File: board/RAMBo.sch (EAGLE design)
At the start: 287 parts, among them Q1 PSMN7R0-60YS, Q2 PSMN7R0-60YS, Q3 PSMN7R0-60YS, Q4 IRLML6346TRPBF, Q5 PSMN7R0-60YS, Q8 IRLML6346TRPBF, U1 ATMEGA32U2-MUR, U10 ADUM7441, U2 ATMEGA2560-16AU, U3 LM22675, U4 AD5206, U5 A4982, U6 A4982, U7 A4982, U8 A4982, U9 A4982, X1 C-GRID-02-70543, X10 C-GRID-04-70543, X11 MSTBV10, X12 SPI, X13 EXT-2, X14 C-GRID-04-70543, X15 C-GRID-04-70543, X16 32u2 EXT, X17 3x2M, X18 3x2M, X2 USB B-TH, X20 MX1, X21 C-GRID-03-70543, X22 C-GRID-03-70543, X23 C-GRID-03-70543, X24 C-GRID-03-70543, X25 C-GRID-03-70543, X26 C-GRID-03-70543, X27 C-GRID-02-70543, X28 C-GRID-02-70543, X29 C-GRID-02-70543, X3 C-GRID-02-70543, X30 C-GRID-02-70543, X31 MX2, X32 MX3, X33 MSTBA6, X34 PWM_EXT, X39 M05X2PTH, X4 C-GRID-04-70543, X40 Analog, X5 C-GRID-02-70543, X6 C-GRID-04-70543, X7 C-GRID-04-70543, X8 C-GRID-04-70543, X9 C-GRID-02-70543, Y1 16MHz KX-7, Y2 16MHz KX-7

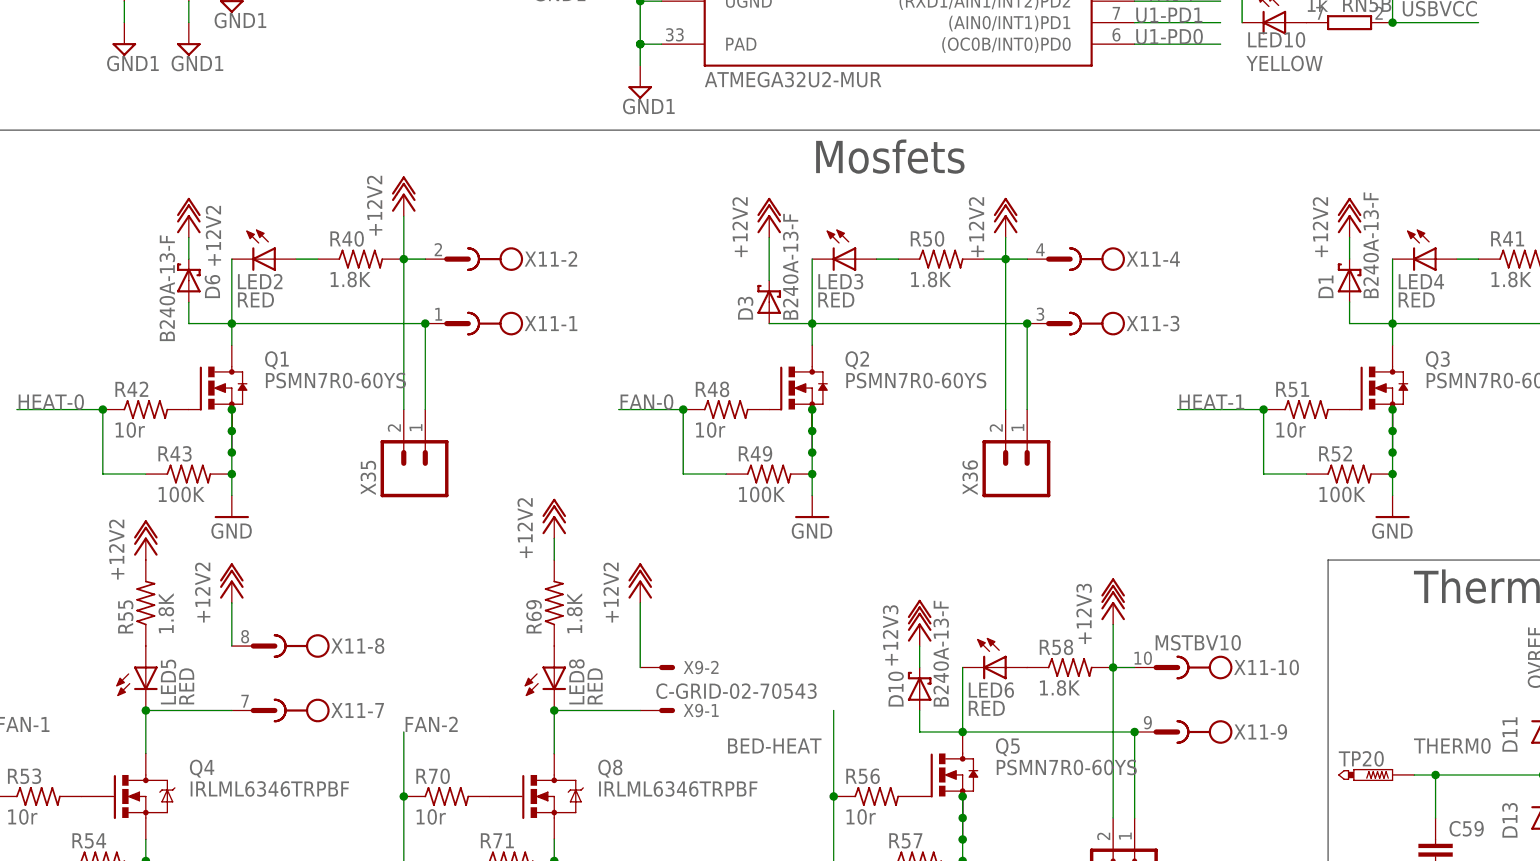
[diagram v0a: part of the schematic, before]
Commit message: Change flyback diodes to SK310A
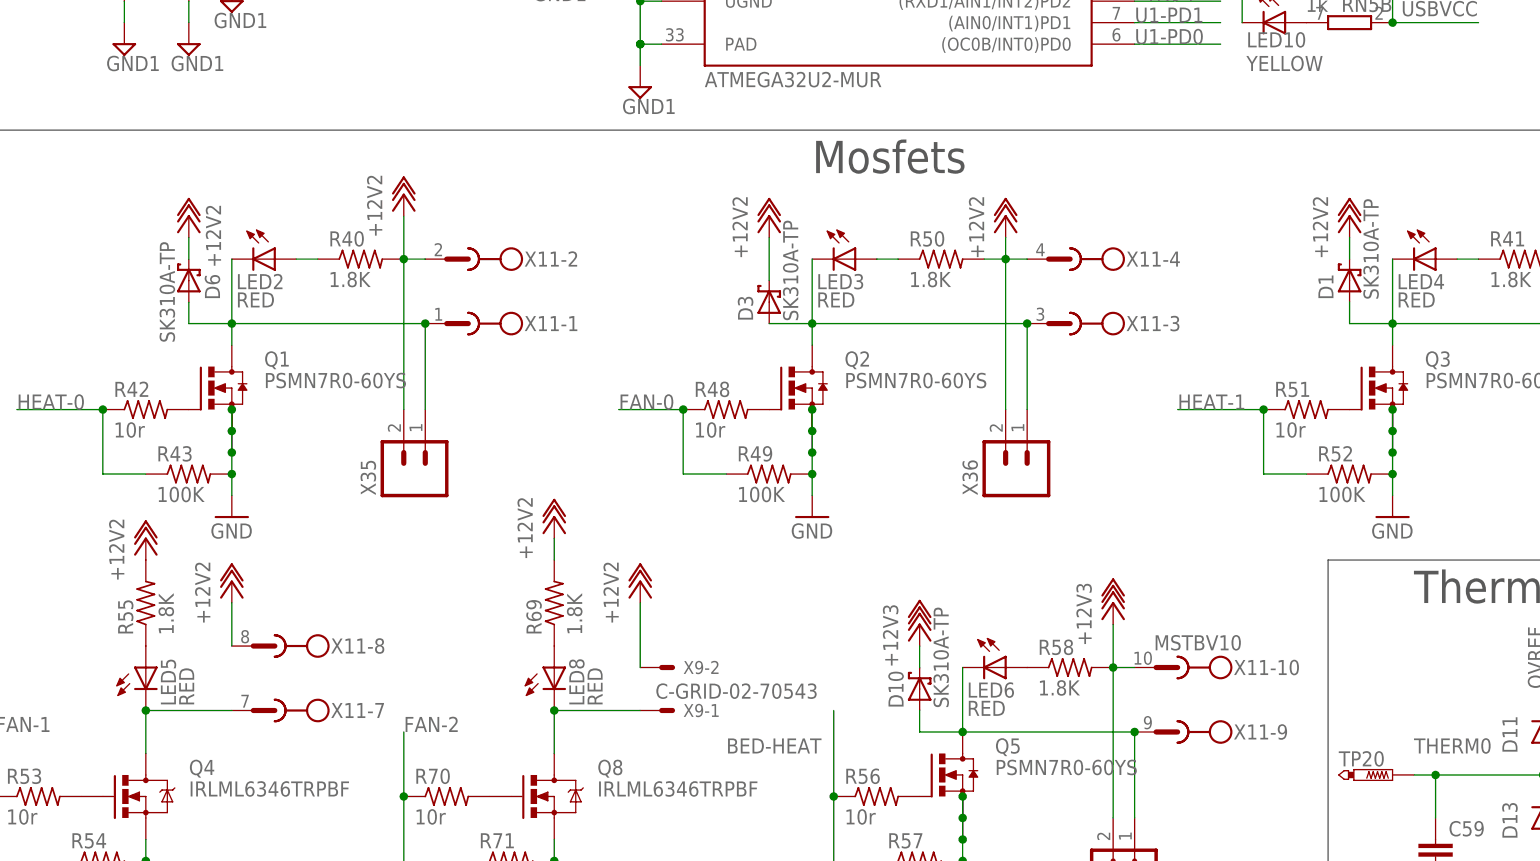
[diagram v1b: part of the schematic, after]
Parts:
- D1, D10, D3, D6: value B240A-13-F -> SK310A-TP
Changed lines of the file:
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@@
 <grid distance="0.1" unitdist="inch" unit="inch" style="lines" multiple="1" display="no" altdistance="0.01" altunitdist="inch" altunit="inch"/>
 <layers>
-<layer number="1" name="Top" color="4" fill="1" visible="yes" active="no"/>
-<layer number="2" name="Route2" color="13" fill="3" visible="yes" active="no"/>
-<layer number="3" name="Route3" color="4" fill="3" visible="yes" active="no"/>
-<layer number="14" name="Route14" color="1" fill="6" visible="yes" active="no"/>
-<layer number="15" name="Route15" color="11" fill="6" visible="yes" active="no"/>
-<layer number="16" name="Bottom" color="1" fill="1" visible="yes" active="no"/>
-<layer number="17" name="Pads" color="2" fill="1" visible="yes" active="no"/>
-<layer number="18" name="Vias" color="2" fill="1" visible="yes" active="no"/>
-<layer number="19" name="Unrouted" color="6" fill="1" visible="yes" active="no"/>
-<layer number="20" name="Dimension" color="15" fill="1" visible="yes" active="no"/>
-<layer number="21" name="tPlace" color="7" fill="1" visible="yes" active="no"/>
-<layer number="22" name="bPlace" color="7" fill="1" visible="yes" active="no"/>
-<layer number="23" name="tOrigins" color="15" fill="1" visible="yes" active="no"/>
-<layer number="24" name="bOrigins" color="15" fill="1" visible="yes" active="no"/>
-<layer number="25" name="tNames" color="7" fill="1" visible="yes" active="no"/>
-<layer number="26" name="bNames" color="7" fill="1" visible="yes" active="no"/>
-<layer number="27" name="tValues" color="7" fill="1" visible="yes" active="no"/>
-<layer number="28" name="bValues" color="7" fill="1" visible="yes" active="no"/>
+<layer number="1" name="Top" color="4" fill="1" visible="no" active="no"/>
+<layer number="2" name="Route2" color="13" fill="3" visible="no" active="no"/>
+<layer number="3" name="Route3" color="4" fill="3" visible="no" active="no"/>
+<layer number="14" name="Route14" color="1" fill="6" visible="no" active="no"/>
+<layer number="15" name="Route15" color="11" fill="6" visible="no" active="no"/>
+<layer number="16" name="Bottom" color="1" fill="1" visible="no" active="no"/>
+<layer number="17" name="Pads" color="2" fill="1" visible="no" active="no"/>
+<layer number="18" name="Vias" color="2" fill="1" visible="no" active="no"/>
+<layer number="19" name="Unrouted" color="6" fill="1" visible="no" active="no"/>
+<layer number="20" name="Dimension" color="15" fill="1" visible="no" active="no"/>
+<layer number="21" name="tPlace" color="7" fill="1" visible="no" active="no"/>
+<layer number="22" name="bPlace" color="7" fill="1" visible="no" active="no"/>
+<layer number="23" name="tOrigins" color="15" fill="1" visible="no" active="no"/>
+<layer number="24" name="bOrigins" color="15" fill="1" visible="no" active="no"/>
+<layer number="25" name="tNames" color="7" fill="1" visible="no" active="no"/>
+<layer number="26" name="bNames" color="7" fill="1" visible="no" active="no"/>
+<layer number="27" name="tValues" color="7" fill="1" visible="no" active="no"/>
+<layer number="28" name="bValues" color="7" fill="1" visible="no" active="no"/>
 <layer number="29" name="tStop" color="7" fill="3" visible="no" active="no"/>
 <layer number="30" name="bStop" color="7" fill="6" visible="no" active="no"/>
@@
 <layer number="35" name="tGlue" color="7" fill="4" visible="no" active="no"/>
 <layer number="36" name="bGlue" color="7" fill="5" visible="no" active="no"/>
-<layer number="37" name="tTest" color="7" fill="1" visible="yes" active="no"/>
-<layer number="38" name="bTest" color="7" fill="1" visible="yes" active="no"/>
+<layer number="37" name="tTest" color="7" fill="1" visible="no" active="no"/>
+<layer number="38" name="bTest" color="7" fill="1" visible="no" active="no"/>
 <layer number="39" name="tKeepout" color="4" fill="11" visible="no" active="no"/>
 <layer number="40" name="bKeepout" color="1" fill="11" visible="no" active="no"/>
@@
 <layer number="44" name="Drills" color="7" fill="1" visible="no" active="no"/>
 <layer number="45" name="Holes" color="7" fill="1" visible="no" active="no"/>
-<layer number="46" name="Milling" color="3" fill="1" visible="yes" active="no"/>
-<layer number="47" name="Measures" color="7" fill="1" visible="yes" active="no"/>
-<layer number="48" name="Document" color="7" fill="1" visible="yes" active="no"/>
-<layer number="49" name="Reference" color="7" fill="1" visible="yes" active="no"/>
-<layer number="50" name="dxf" color="12" fill="1" visible="yes" active="no"/>
-<layer number="51" name="tDocu" color="7" fill="1" visible="yes" active="no"/>
-<layer number="52" name="bDocu" color="7" fill="1" visible="yes" active="no"/>
-<layer number="53" name="tGND_GNDA" color="7" fill="1" visible="yes" active="no"/>
-<layer number="54" name="bGND_GNDA" color="7" fill="1" visible="yes" active="no"/>
-<layer number="56" name="wert" color="7" fill="1" visible="yes" active="no"/>
+<layer number="46" name="Milling" color="3" fill="1" visible="no" active="no"/>
+<layer number="47" name="Measures" color="7" fill="1" visible="no" active="no"/>
+<layer number="48" name="Document" color="7" fill="1" visible="no" active="no"/>
+<layer number="49" name="Reference" color="7" fill="1" visible="no" active="no"/>
+<layer number="50" name="dxf" color="12" fill="1" visible="no" active="no"/>
+<layer number="51" name="tDocu" color="7" fill="1" visible="no" active="no"/>
+<layer number="52" name="bDocu" color="7" fill="1" visible="no" active="no"/>
+<layer number="53" name="tGND_GNDA" color="7" fill="1" visible="no" active="no"/>
+<layer number="54" name="bGND_GNDA" color="7" fill="1" visible="no" active="no"/>
+<layer number="56" name="wert" color="7" fill="1" visible="no" active="no"/>
 <layer number="91" name="Nets" color="2" fill="1" visible="yes" active="yes"/>
 <layer number="92" name="Busses" color="1" fill="1" visible="yes" active="yes"/>
@@
 <part name="FID1" library="SparkFun" deviceset="FIDUCIAL" device="1X2"/>
 <part name="FID3" library="SparkFun" deviceset="FIDUCIAL" device="1X2"/>
-<part name="D1" library="ultimachine1" deviceset="SCHOTTKY-DIODE" device="" value="B240A-13-F"/>
-<part name="D3" library="ultimachine1" deviceset="SCHOTTKY-DIODE" device="" value="B240A-13-F"/>
-<part name="D6" library="ultimachine1" deviceset="SCHOTTKY-DIODE" device="" value="B240A-13-F"/>
-<part name="D10" library="ultimachine1" deviceset="SCHOTTKY-DIODE" device="" value="B240A-13-F"/>
+<part name="D1" library="ultimachine1" deviceset="SCHOTTKY-DIODE" device="" value="SK310A-TP"/>
+<part name="D3" library="ultimachine1" deviceset="SCHOTTKY-DIODE" device="" value="SK310A-TP"/>
+<part name="D6" library="ultimachine1" deviceset="SCHOTTKY-DIODE" device="" value="SK310A-TP"/>
+<part name="D10" library="ultimachine1" deviceset="SCHOTTKY-DIODE" device="" value="SK310A-TP"/>
 <part name="U10" library="ultimachine" deviceset="ADUM7441" device=""/>
 <part name="P+72" library="supply1" deviceset="VCC" device=""/>

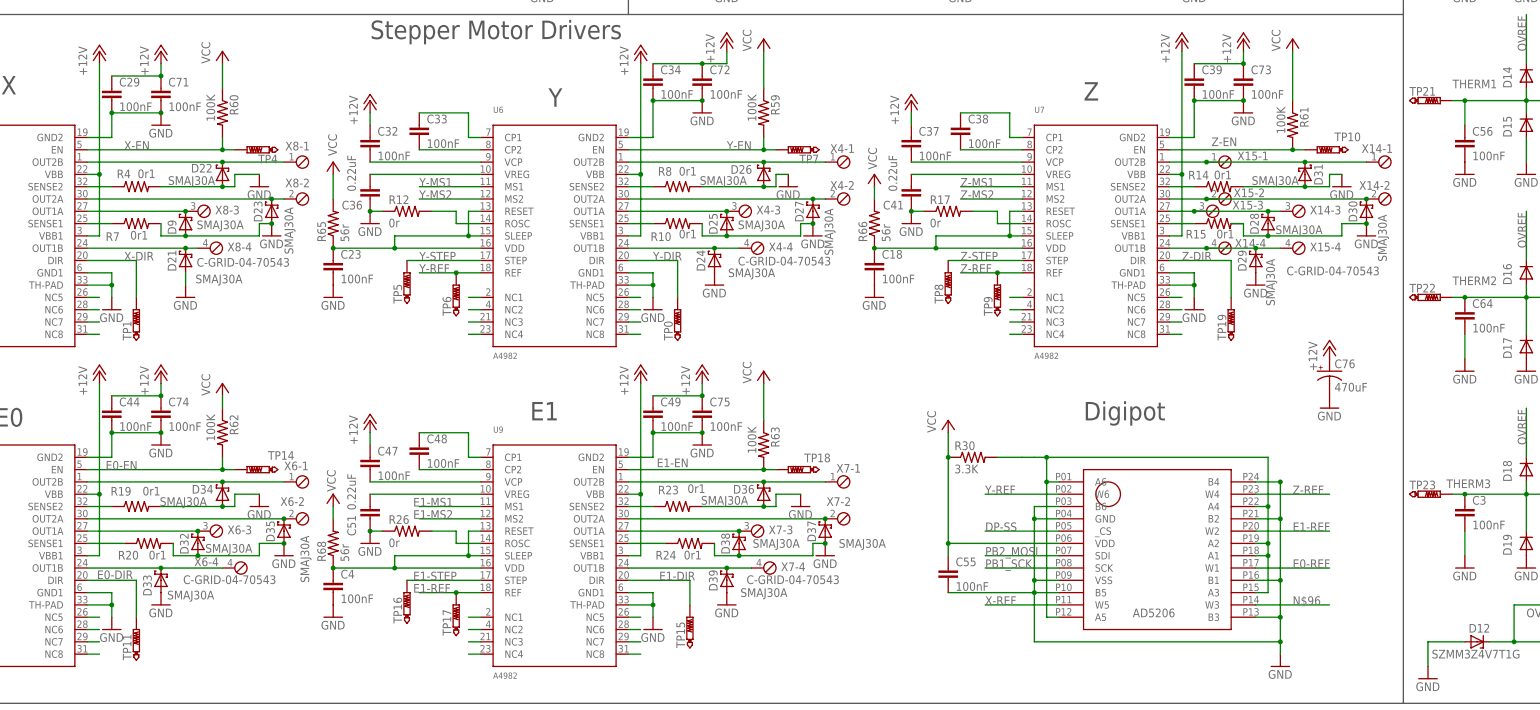
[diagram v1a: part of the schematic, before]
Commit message: Add EMFIL pass through caps to motor outputs
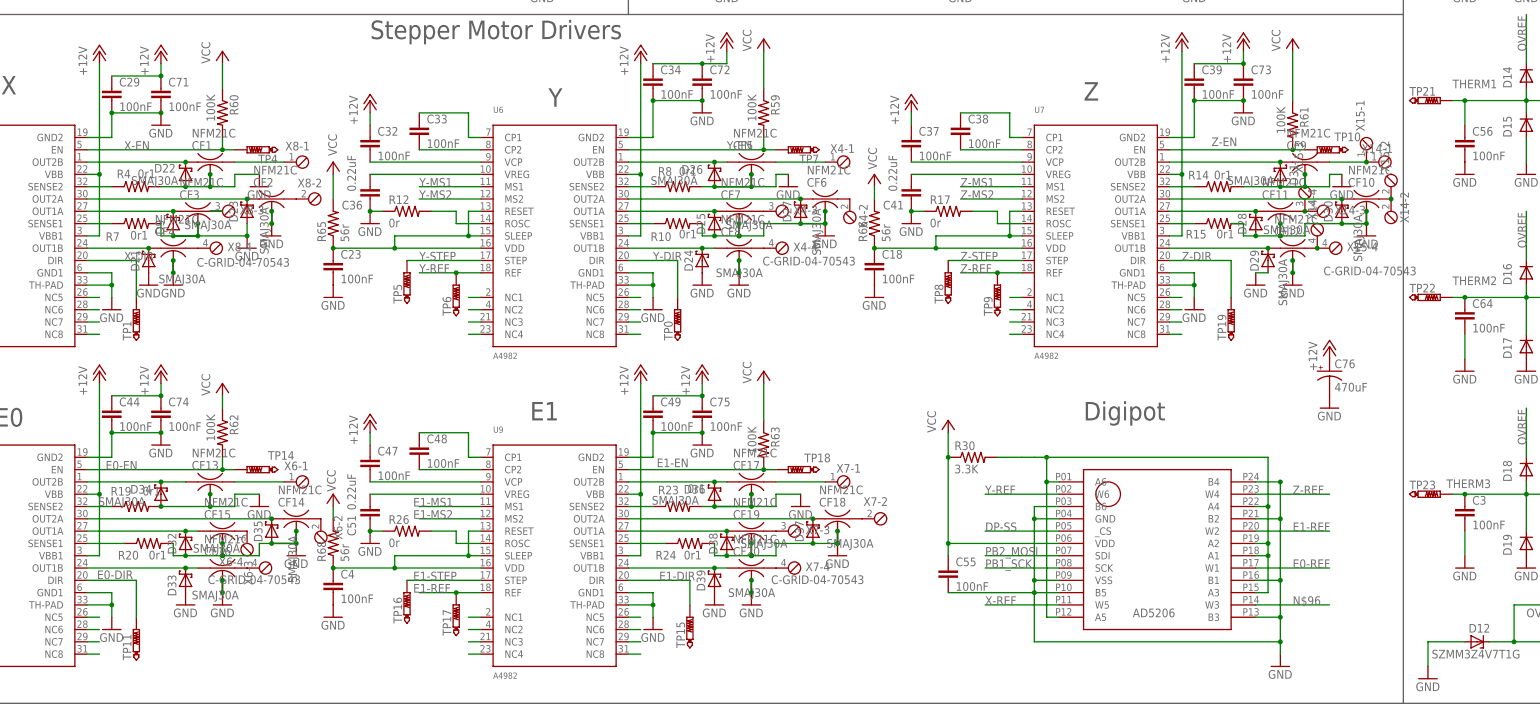
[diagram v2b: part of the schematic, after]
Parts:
- added CF1, CF10, CF11, CF12, CF13, CF14, CF15, CF16, CF17, CF18, CF19, CF2, CF20, CF3, CF4, CF5, CF6, CF7, CF8, CF9: NFM21C, murata-filter:NFM21C
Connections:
- removed net N$51: D23.C, U5.OUT2A, X8-2.1
- new net N$111: CF14.3, X6-2.1
- new net N$115: CF16.1, D33.C, U8.OUT1B
- new net N$116: CF4.3, X8-4.1
- new net N$119: CF3.3, X8-3.1
- new net N$121: CF2.3, X8-2.1
- new net N$142: CF1.3, X8-1.1
- new net N$153: CF8.3, X4-4.1
- new net N$161: CF7.3, X4-3.1
- new net N$166: CF6.3, X4-2.1
- new net N$167: CF8.1, D24.C, U6.OUT1B
- new net N$168: CF9.1, D31.C, U7.OUT2B
- new net N$169: CF11.3, X14-3.1, X15-3.1
- new net N$170: CF9.3, X14-1.1, X15-1.1
- new net N$171: CF10.3, X14-2.1, X15-2.1
- new net N$173: CF2.1, D23.C, U5.OUT2A
- new net N$18: CF20.3, X7-4.1
- new net N$39: CF19.3, X7-3.1
- new net N$65: CF18.3, X7-2.1
- new net N$93: CF17.3, X7-1.1
- new net N$94: CF16.3, X6-4.1
- new net N$97: CF15.3, X6-3.1
- net GND: now also CF1.2@1, CF1.2@2, CF10.2@1, CF10.2@2, CF11.2@1, CF11.2@2, CF12.2@1, CF12.2@2, CF13.2@1, CF13.2@2, CF14.2@1, CF14.2@2, CF15.2@1, CF15.2@2, CF16.2@1, CF16.2@2, CF17.2@1, CF17.2@2, CF18.2@1, CF18.2@2, CF19.2@1, CF19.2@2, CF2.2@1, CF2.2@2, CF20.2@1, CF20.2@2, CF3.2@1, CF3.2@2, CF4.2@1, CF4.2@2, CF5.2@1, CF5.2@2, CF6.2@1, CF6.2@2, CF7.2@1, CF7.2@2, CF8.2@1, CF8.2@2, CF9.2@1, CF9.2@2
- net N$17: now also CF5.1, D26.C, U6.OUT2B; no longer D27.C, U6.OUT2A, X4-2.1
- net N$19: now also CF5.3, X4-1.1; no longer D25.C, U6.OUT1A, X4-3.1
- net N$20: now also CF6.1, D27.C, U6.OUT2A; no longer D24.C, U6.OUT1B, X4-4.1
- net N$23: now also CF7.1, D25.C, U6.OUT1A; no longer D26.C, U6.OUT2B, X4-1.1
- net N$34: now also CF10.1; no longer X14-2.1, X15-2.1
- net N$35: now also CF11.1; no longer X14-3.1, X15-3.1
- net N$40: now also CF12.1; no longer X14-4.1, X15-4.1
- net N$41: now also CF12.3, X14-4.1, X15-4.1; no longer D31.C, U7.OUT2B, X14-1.1, X15-1.1
- net N$47: now also CF1.1; no longer X8-1.1
- net N$52: now also CF3.1; no longer X8-3.1
- net N$53: now also CF4.1; no longer X8-4.1
- net N$59: now also CF13.1, D34.C, U8.OUT2B; no longer D35.C, U8.OUT2A, X6-2.1
- net N$60: now also CF13.3, X6-1.1; no longer D32.C, U8.OUT1A, X6-3.1
- net N$61: now also CF14.1, D35.C, U8.OUT2A; no longer D33.C, U8.OUT1B, X6-4.1
- net N$62: now also CF15.1, D32.C, U8.OUT1A; no longer D34.C, U8.OUT2B, X6-1.1
- net N$72: now also CF20.1, D39.C, U9.OUT1B; no longer D37.C, U9.OUT2A, X7-2.1
- net N$73: now also CF19.1; no longer X7-3.1
- net N$74: now also CF17.1, D36.C, U9.OUT2B; no longer D39.C, U9.OUT1B, X7-4.1
- net N$75: now also CF18.1, D37.C, U9.OUT2A; no longer D36.C, U9.OUT2B, X7-1.1
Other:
- moved on the sheet: D21, D22, D23, D24, D25, D26, D27, D28, D29, D30, D31, D32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
